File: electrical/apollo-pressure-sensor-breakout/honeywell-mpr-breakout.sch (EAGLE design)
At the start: 8 parts, among them U1 HONEYWELL-MPR-SMD-GAUGE, X1 RJ45-8-2-CONEC-1, X2 M04X2

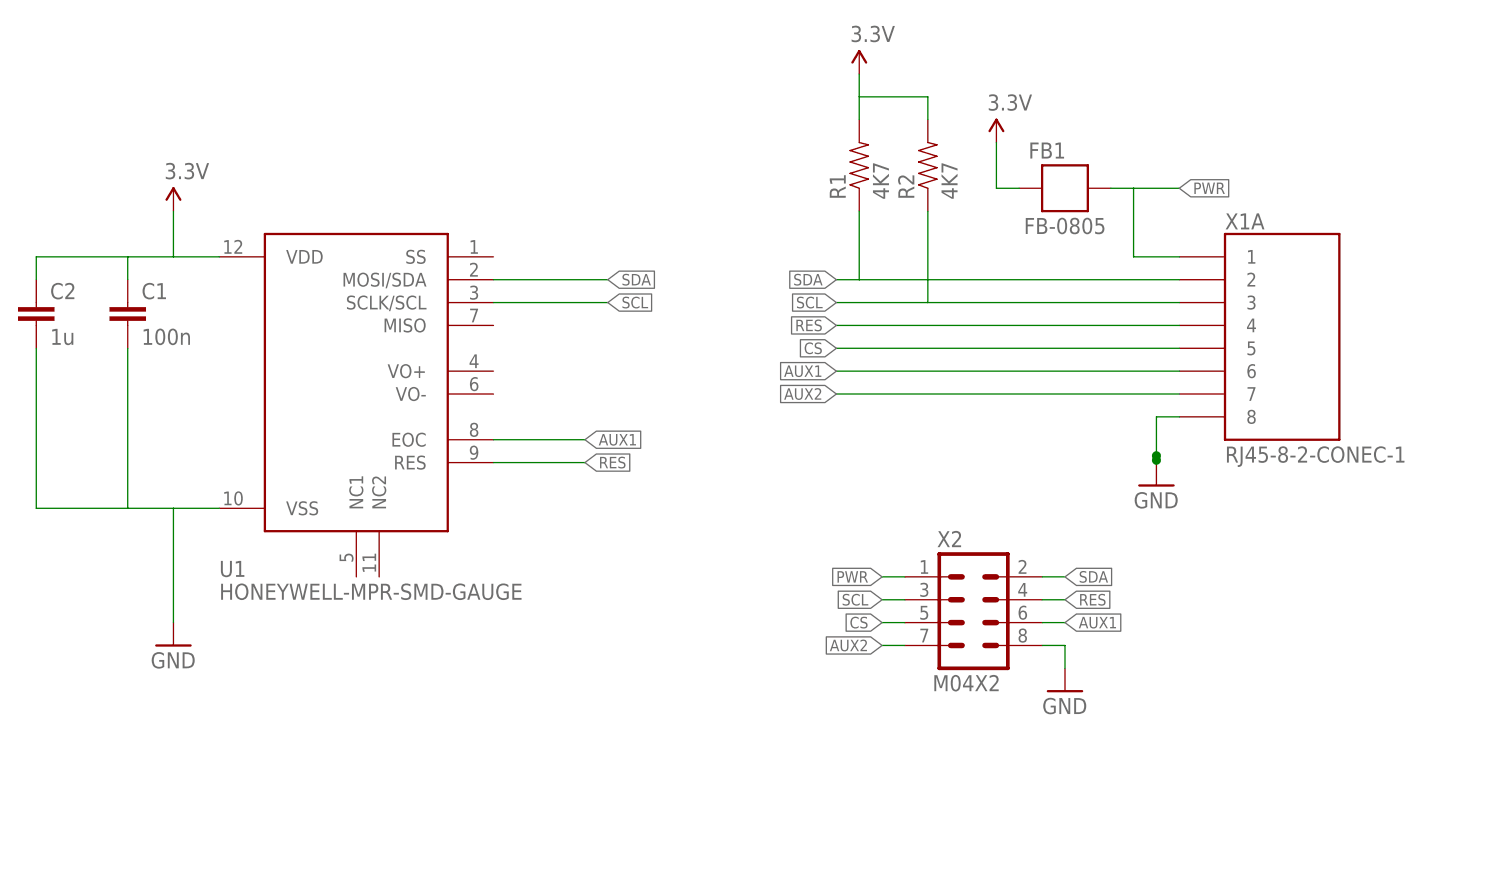
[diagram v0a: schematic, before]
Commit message: add Gerber/SMTA order info for JLCPCB
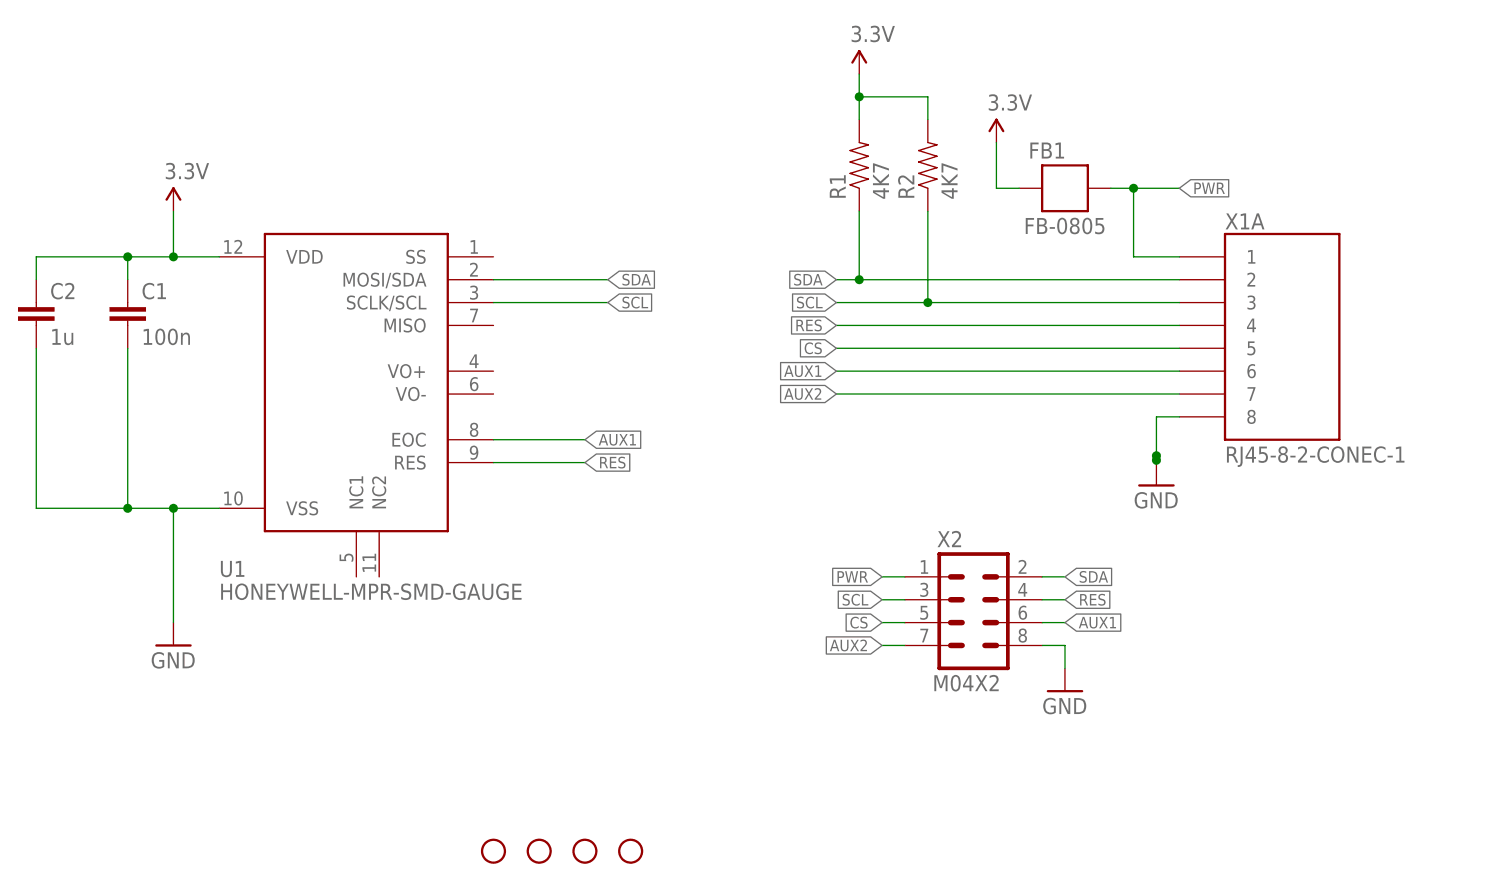
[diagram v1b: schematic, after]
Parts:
- added JP1, JP2, JP3, JP4: STAND-OFF, apollo-ctrl:STAND-OFF

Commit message: added SPI signals to MPR breakout
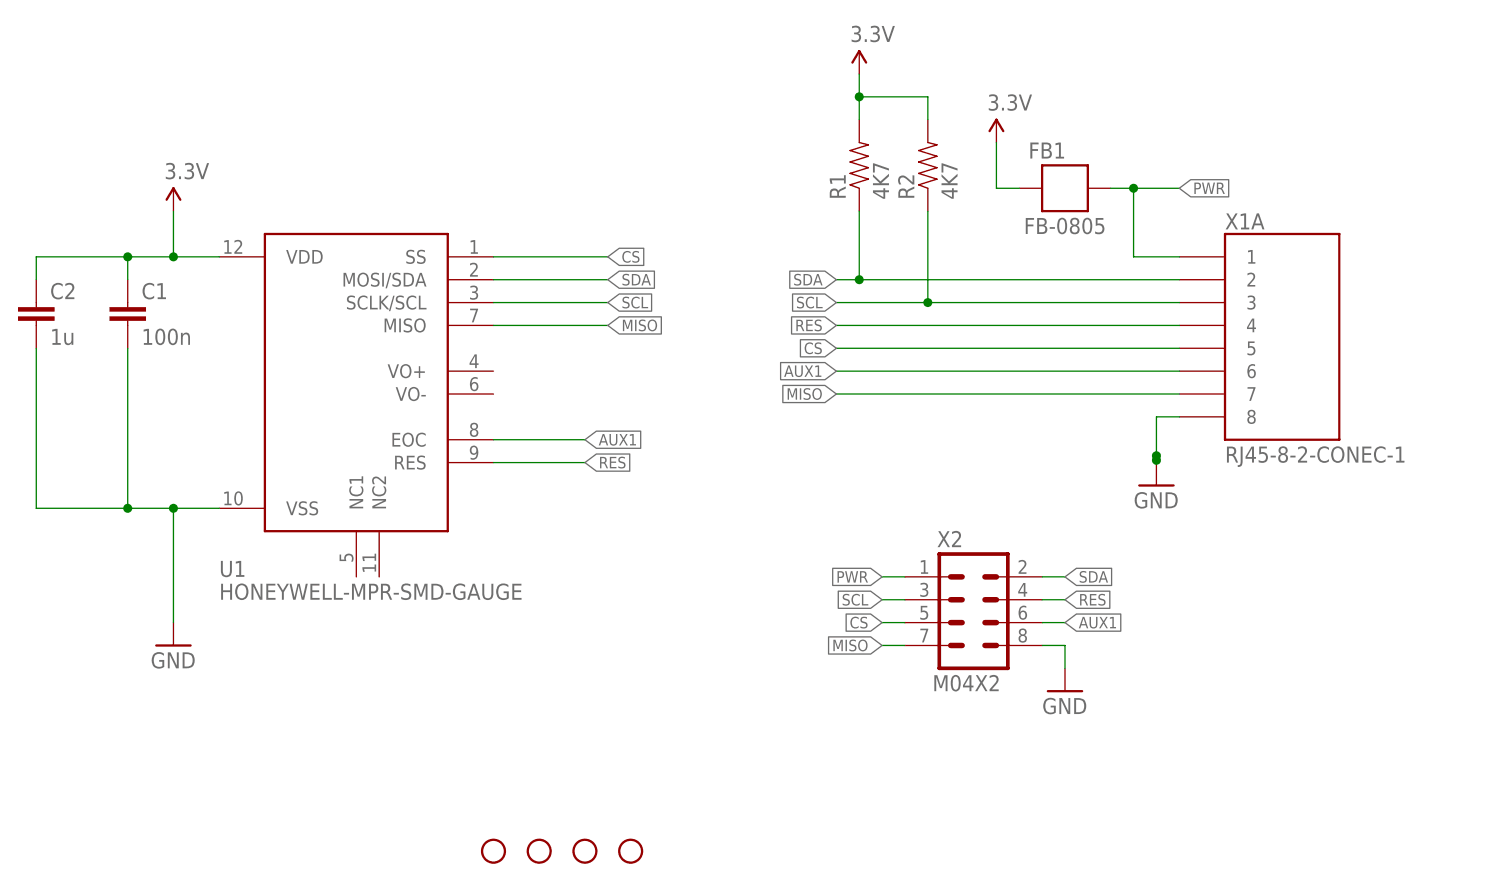
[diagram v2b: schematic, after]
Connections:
- removed net AUX2: X1A.7, X2.7
- new net MISO: U1.MISO, X1A.7, X2.7
- net CS: now also U1.SS
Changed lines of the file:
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@@
 <?xml version="1.0" encoding="utf-8"?>
 <!DOCTYPE eagle SYSTEM "eagle.dtd">
-<eagle version="9.3.0">
+<eagle version="7.6.0">
 <drawing>
 <settings>
 <setting alwaysvectorfont="no"/>
-<setting keepoldvectorfont="yes"/>
 <setting verticaltext="up"/>
 </settings>
@@
 <label x="124.46" y="17.78" size="1.27" layer="95" rot="R180" xref="yes"/>
 </segment>
+<segment>
+<pinref part="U1" gate="G$1" pin="SS"/>
+<wire x1="81.28" y1="58.42" x2="93.98" y2="58.42" width="0.1524" layer="91"/>
+<label x="93.98" y="58.42" size="1.27" layer="95" xref="yes"/>
+</segment>
 </net>
 <net name="AUX1" class="0">
@@
 </segment>
 </net>
-<net name="AUX2" class="0">
+<net name="MISO" class="0">
+<segment>
+<pinref part="U1" gate="G$1" pin="MISO"/>
+<wire x1="81.28" y1="50.8" x2="93.98" y2="50.8" width="0.1524" layer="91"/>
+<label x="93.98" y="50.8" size="1.27" layer="95" xref="yes"/>
+</segment>
 <segment>
 <pinref part="X1" gate="A" pin="7"/>
